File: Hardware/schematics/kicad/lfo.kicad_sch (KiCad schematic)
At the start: 28 parts, among them U12 Electric Druid TAPLFO 3, U13 AS3360, U14 L7905, U5 TL074HID

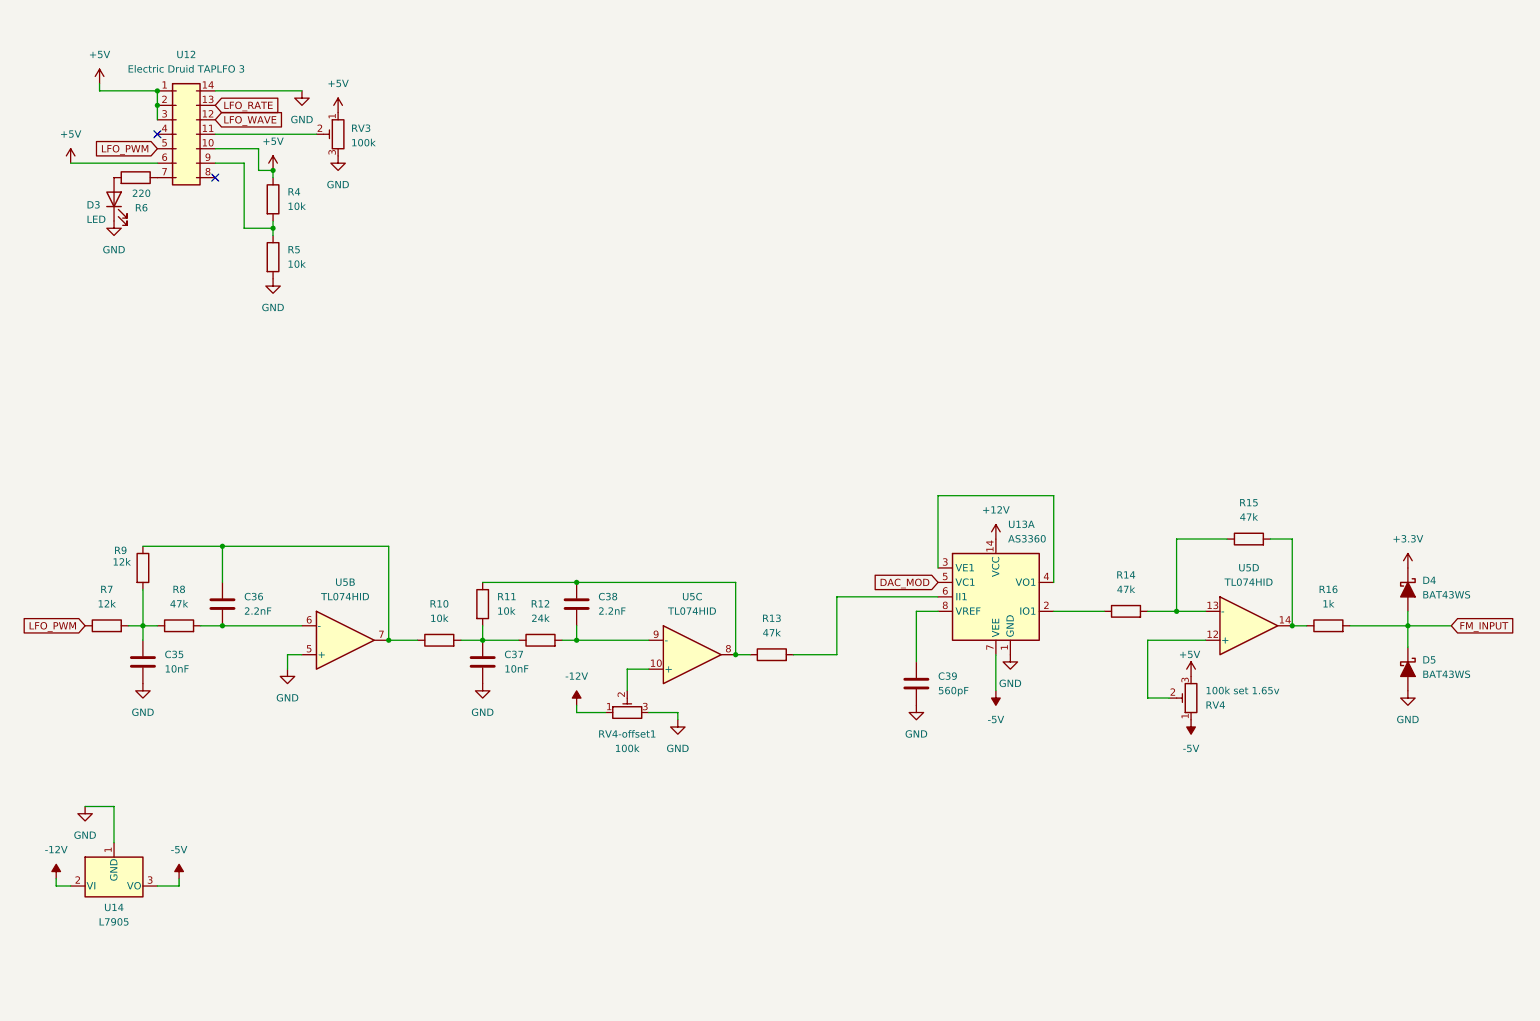
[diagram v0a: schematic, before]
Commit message: Modify schematics to suit a complete Eurorack PCB design
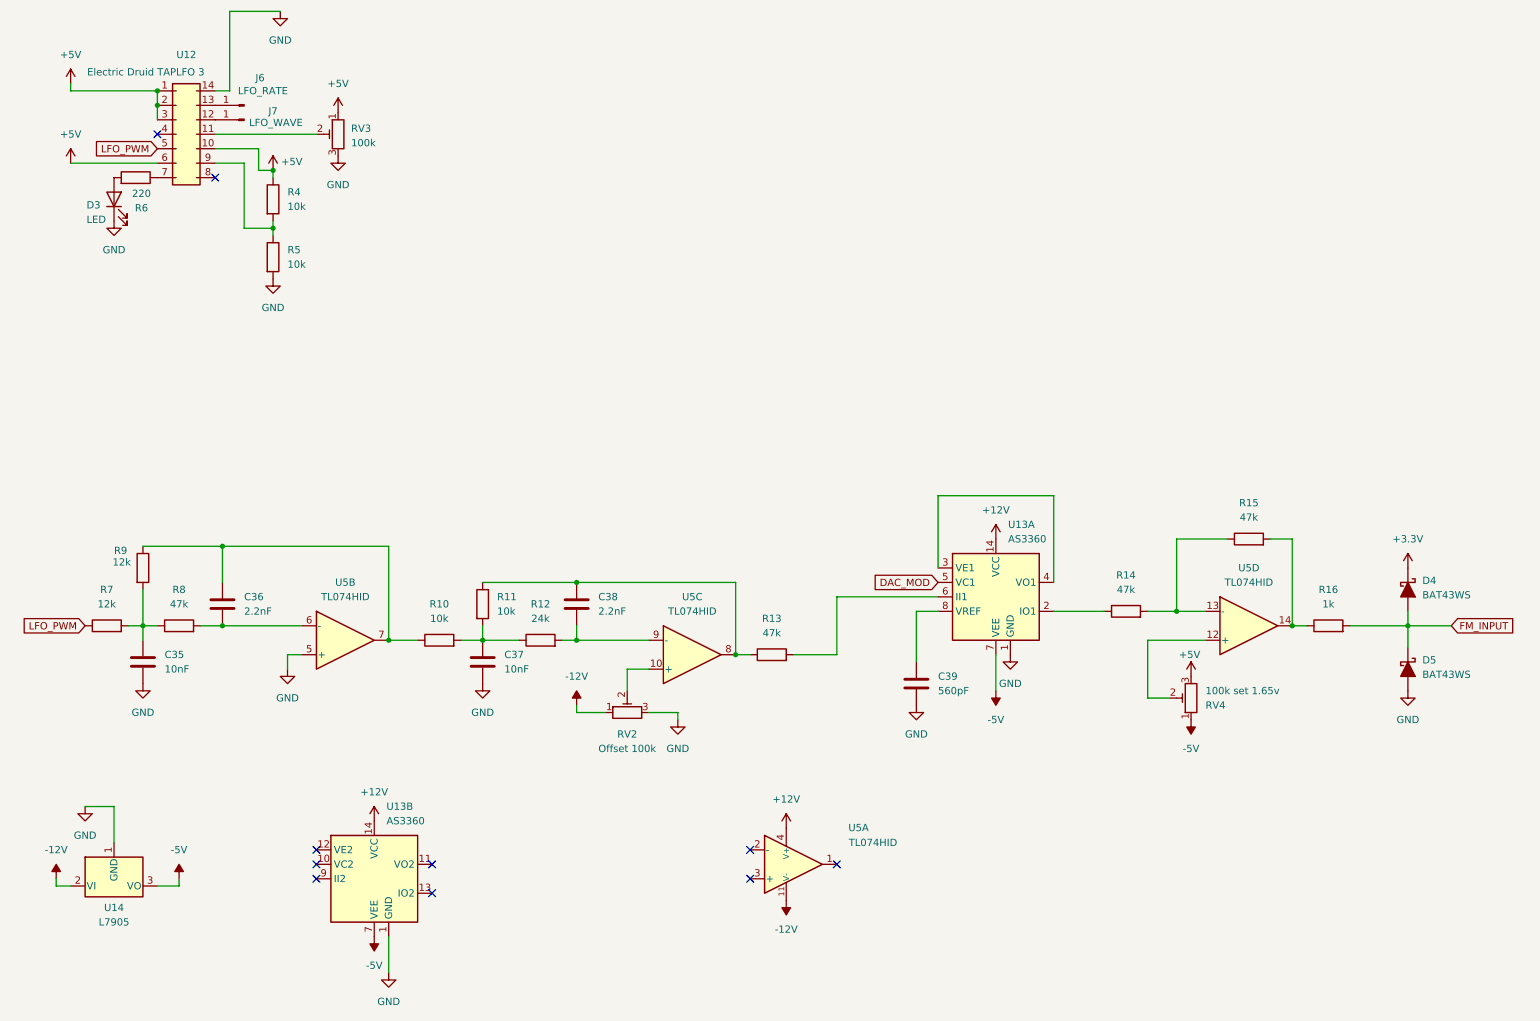
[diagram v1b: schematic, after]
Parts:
- added J6: LFO_RATE, Connector_Wire:SolderWirePad_1x01_SMD_2x4mm, symbol Connector:Conn_01x01_Pin
- added J7: LFO_WAVE, Connector_Wire:SolderWirePad_1x01_SMD_2x4mm, symbol Connector:Conn_01x01_Pin
- added unit 2 of U13
- added unit 1 of U5
- RV2: renamed from RV4-offset1; value 100k -> Offset 100k
- RV4: footprint PCM_Potentiometer_THT_AKL:Potentiometer_Runtron_RM-065_Vertical -> Pot-User:Potentiometer_Bourns_3296W_Vertical-User
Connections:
- net +12V: now also U13.14 (VCC), U5.4 (V+)
- net -12V: now also U5.11 (V-)
- net -5V: now also U13.7 (VEE)
- net GND: now also U13.1 (GND)
- net LFO_RATE: no longer names the net of U12.13 (R2.2)
- net LFO_RATE: now also J6.1 (Pin_1)
- net LFO_WAVE: no longer names the net of U12.12 (R3.2)
- net LFO_WAVE: now also J7.1 (Pin_1)
- no-connect marks 2 -> 10

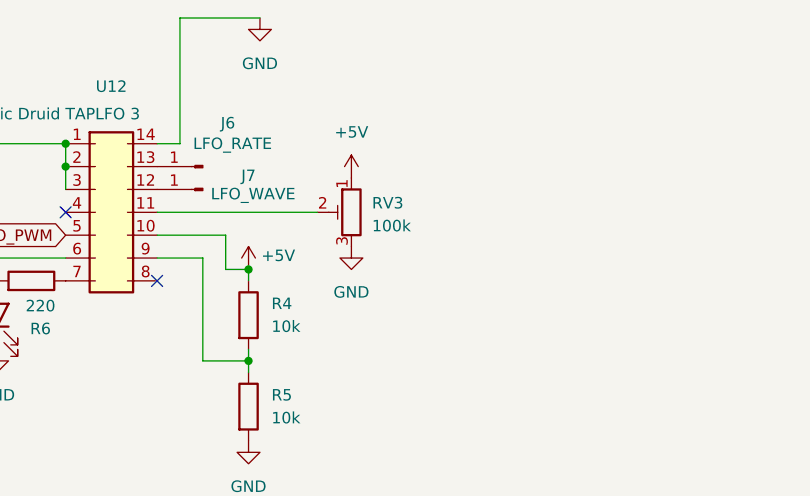
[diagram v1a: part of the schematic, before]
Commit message: Fix schematic bug
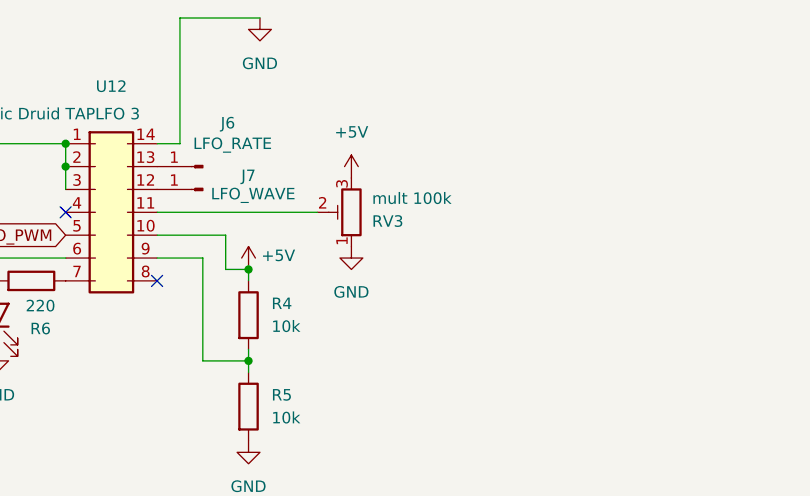
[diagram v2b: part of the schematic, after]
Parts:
- RV3: value 100k -> mult 100k
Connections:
- net +5V: now also RV3.3; no longer RV3.1
- net GND: now also RV3.1; no longer RV3.3
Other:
- moved on the sheet: RV3
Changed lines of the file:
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@@
 	(symbol
 		(lib_id "Device:R_Potentiometer_Trim")
-		(at 76.2 36.83 0)
-		(mirror y)
+		(at 76.2 36.83 180)
 		(unit 1)
 		(exclude_from_sim no)
@@
 		(dnp no)
 		(property "Reference" "RV3"
-			(at 78.486 35.814 0)
+			(at 78.486 37.846 0)
 			(effects
 				(font
@@
 			)
 		)
-		(property "Value" "100k"
-			(at 78.486 38.354 0)
+		(property "Value" "mult 100k"
+			(at 78.486 35.306 0)
 			(effects
 				(font
